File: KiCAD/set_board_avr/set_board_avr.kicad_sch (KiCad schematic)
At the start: 35 parts, among them J1 Conn_01x10, J2 AVR-ISP-6, J3 RJ45, Q1 Q_NPN, Q2 Q_NPN, Q3 Q_NPN, U1 ATtiny4313-S, U4 74HC14, U5 NCP1117-3.3_SOT223

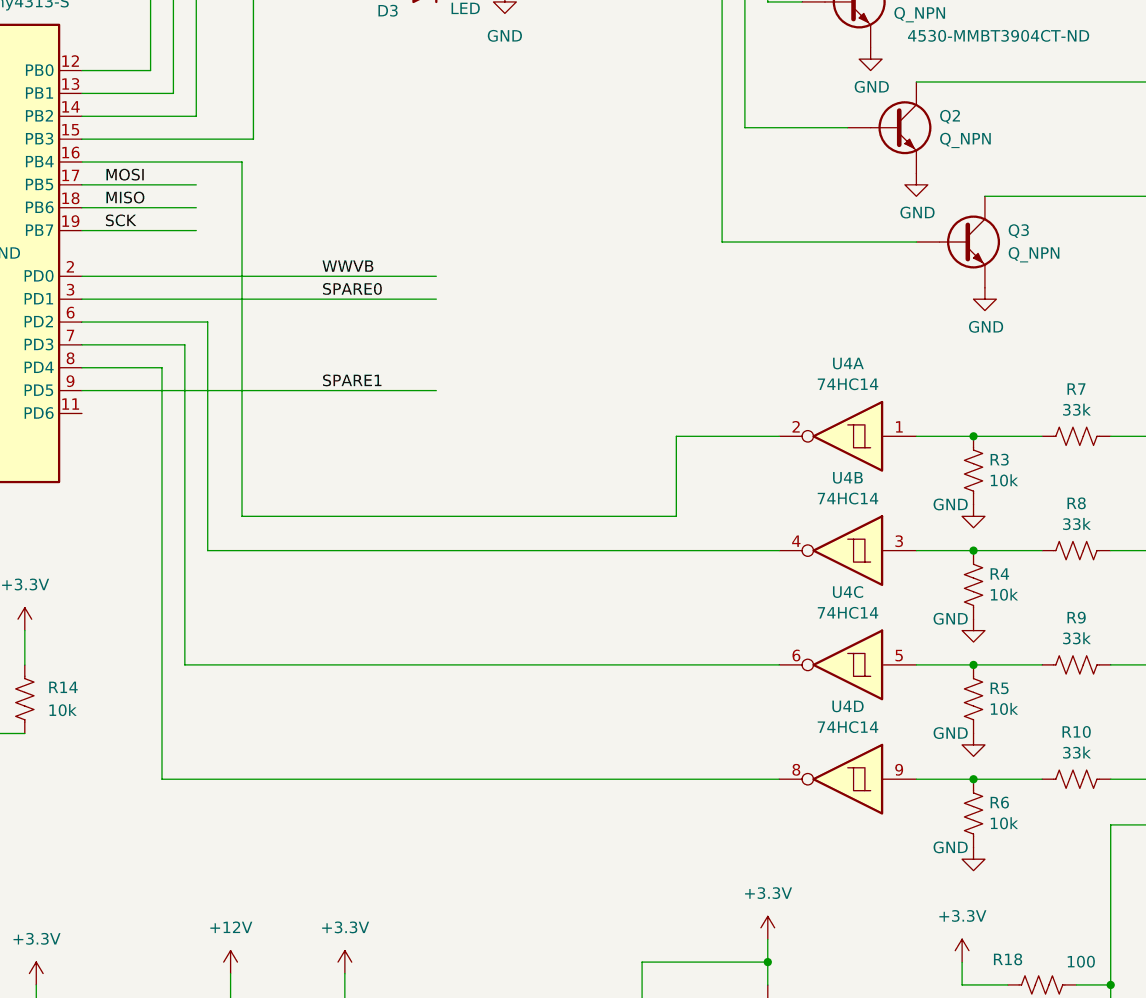
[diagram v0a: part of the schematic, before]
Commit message: maybe add BAV99 protection diodes?
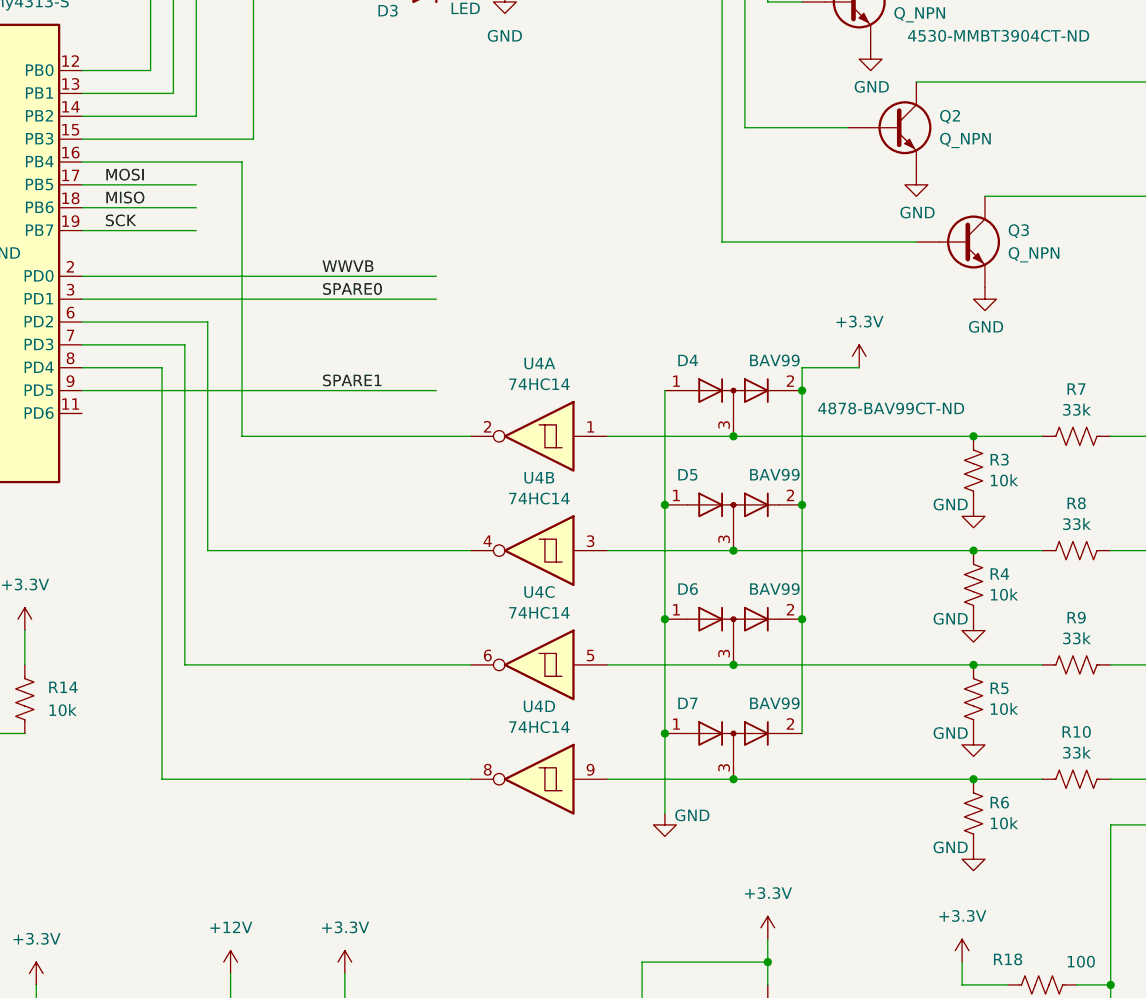
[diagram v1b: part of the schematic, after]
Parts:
- added D4, D5, D6, D7: BAV99, Package_TO_SOT_SMD:SOT-23, symbol Diode:BAV99
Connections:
- net +3.3V: now also D4.2 (A), D5.2 (A), D6.2 (A), D7.2 (A)
- net GND: now also D4.1 (K), D5.1 (K), D6.1 (K), D7.1 (K)
- net at R10.2, R6.1, U4.9: now also D7.3 (K)
- net at R3.1, R7.2, U4.1: now also D4.3 (K)
- net at R4.1, R8.2, U4.3: now also D5.3 (K)
- net at R5.1, R9.2, U4.5: now also D6.3 (K)
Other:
- moved on the sheet: U4A, U4B, U4C, U4D
